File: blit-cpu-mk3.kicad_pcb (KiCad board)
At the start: 4 copper layers, 100 x 80 mm, 169 parts, among them J1 SYS, J11 nML out, J12 nVP out, J13 phi1/abort, J14 nSO in, J16 SYS AUX, J31 HDMI_C_1.3, J32 sound, J33 soundraw, J41 μSD, J44 i2c, J51 rpi_gpio, J52 Conn_02x20_Odd_Even, J54 Conn_02x08_Odd_Even, J56 BOOT, J57 rpi power, J81 JTAG, J82 Jumper, J91 AUX/SYS PWR, J92 AUX PWR, SW611 user0, SW612 user1, SW81 nConfig, U11 74LVC4245A, U12 74LVC4245A, U13 74LVC4245A, U14 74LVC4245A, U21 sst39x040, U22 generic_2048x8_TSOP_II_44, U23 generic_2048x8_TSOP_II_44, U24 generic_2048x8_TSOP_II_44, U25 generic_2048x8_TSOP_II_44, U31 tpd12s016, U42 24AA64-I_OT, U43 rtc_mc_rv_8263_c7, U51 74LVC4245A, U52 74LVC4245A, U53 74CB3T16211, U54 74CB3T16211, U55 74CB3T16211, U8 10M16DCF256I7G_mk3pinstest, U91 stm795, U92 TPS3808, U93 LM1117-1.2, U94 LM1117-2.5, U95 LM1117-3.3, X96 SIT1602BC-23-25N-48.000000

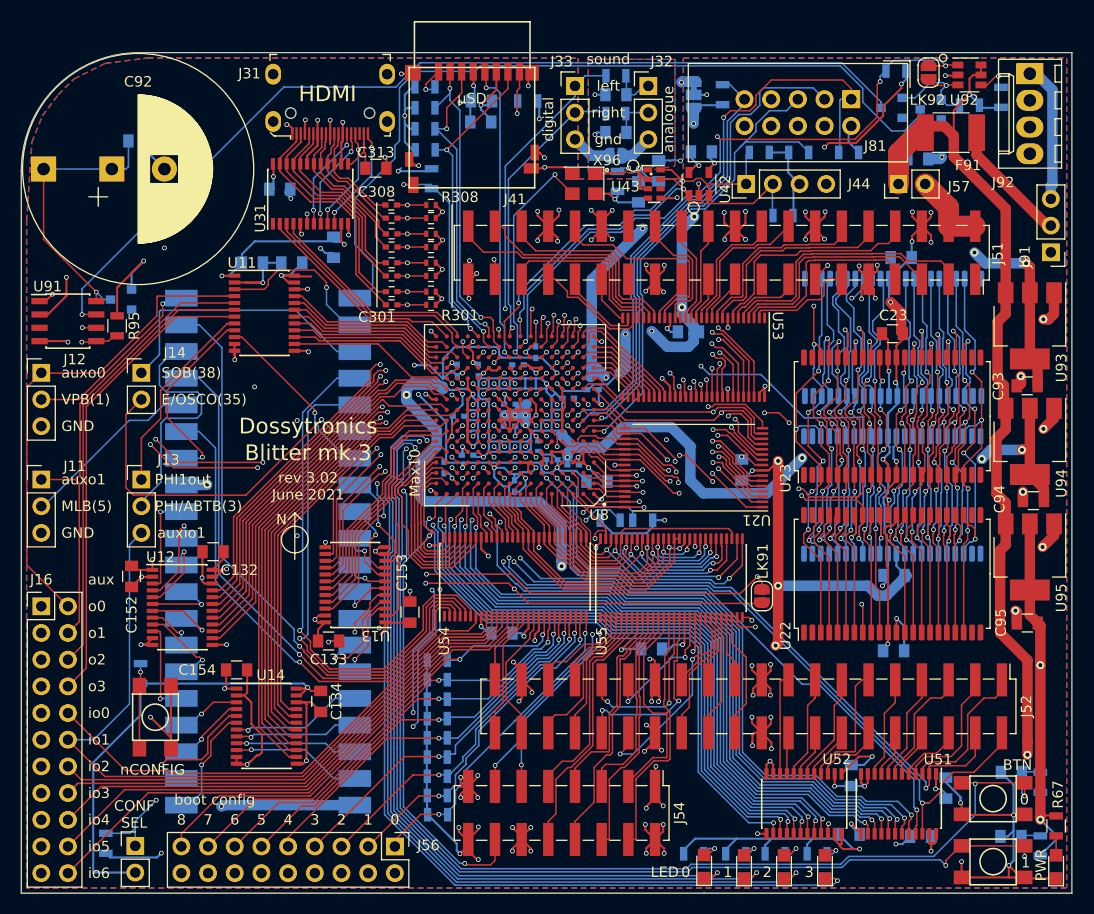
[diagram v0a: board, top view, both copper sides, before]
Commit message: Mk.3 fixes and new 68000 expansion board
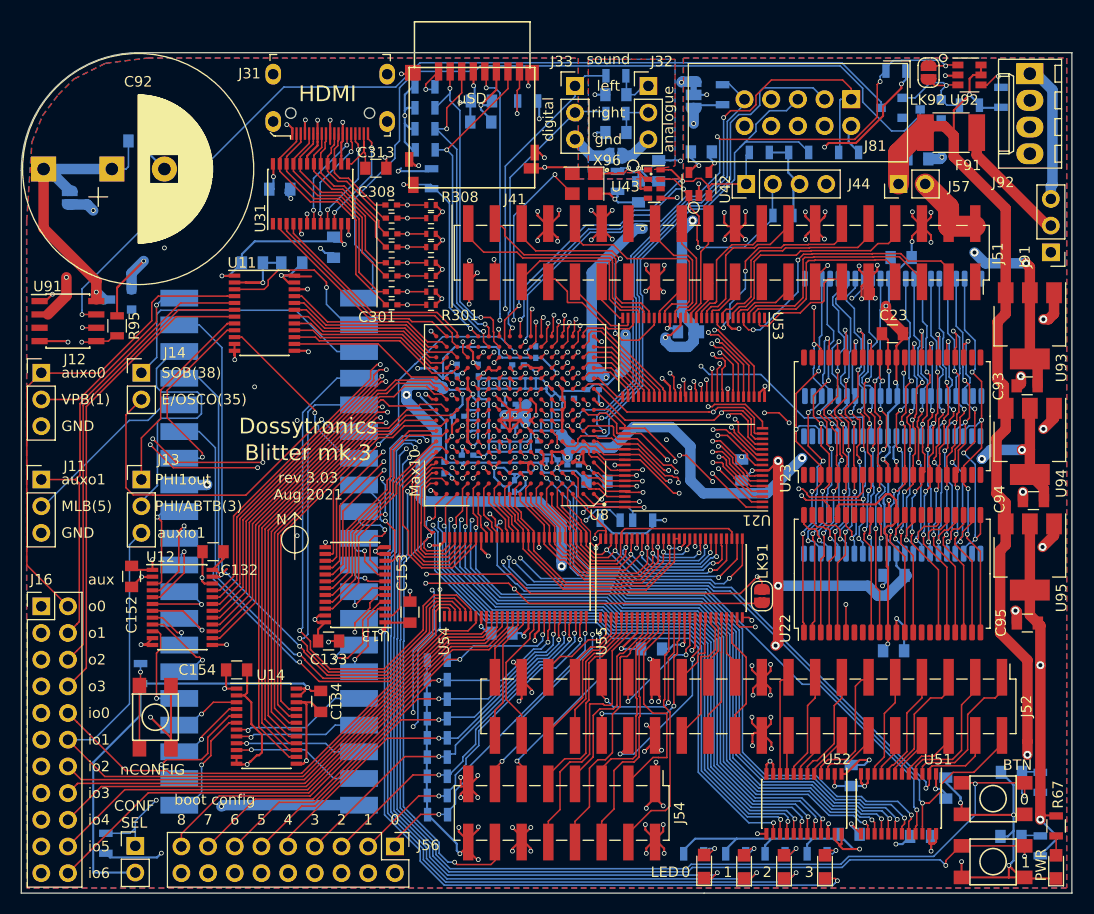
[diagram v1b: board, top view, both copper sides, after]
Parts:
- added LK90: NF, mk3blit:SolderJumper-2_P1.3mm_Open_RoundedPad1.0x1.5mm-domsmallctyd, B.Cu at (26.6, 35.8)
- R63, R64, R65, R66, R67: value 4k7 -> 2k2
- U22: value generic_2048x8_TSOP_II_44 -> generic_2048x8_TSOP_II_44_BB
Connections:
- U22 pad 1: Net-(U22-Pad1) -> /memory/MEM_A14
- U22 pad 15: /MEM_nWE -> Net-(U22-Pad15)
- U22 pad 16: /memory/MEM_A3 -> Net-(U22-Pad16)
- U22 pad 17: /memory/MEM_A2 -> /MEM_nWE
- U22 pad 18: /memory/MEM_A1 -> /memory/MEM_A3
- U22 pad 19: /memory/MEM_A0 -> /memory/MEM_A2
- U22 pad 2: Net-(U22-Pad2) -> /memory/MEM_A13
- U22 pad 20: /memory/MEM_A10 -> /memory/MEM_A1
- U22 pad 21: Net-(U22-Pad21) -> /memory/MEM_A0
- U22 pad 22: Net-(U22-Pad22) -> /memory/MEM_A10
- U22 pad 23: Net-(U22-Pad23) -> /memory/MEM_A19
- U22 pad 24: Net-(U22-Pad24) -> /memory/MEM_A4
- U22 pad 25: /memory/MEM_A19 -> /memory/MEM_A5
- U22 pad 26: /memory/MEM_A4 -> /memory/MEM_A6
- U22 pad 27: /memory/MEM_A5 -> /memory/MEM_A7
- U22 pad 28: /memory/MEM_A6 -> /memory/MEM_A12
- U22 pad 29: /memory/MEM_A7 -> Net-(U22-Pad29)
- U22 pad 3: /memory/MEM_A14 -> /memory/MEM_A8
- U22 pad 30: /memory/MEM_A12 -> Net-(U22-Pad30)
- U22 pad 37: /MEM_nOE -> Net-(U22-Pad37)
- U22 pad 38: /memory/MEM_A17 -> Net-(U22-Pad38)
- U22 pad 39: /memory/MEM_A15 -> /memory/MEM_A17
- U22 pad 4: /memory/MEM_A13 -> /memory/MEM_A9
- U22 pad 40: /memory/MEM_A16 -> /memory/RAM0PWR
- U22 pad 41: /memory/MEM_A18 -> /MEM_nOE
- U22 pad 42: /memory/MEM_A20 -> /memory/MEM_A15
- U22 pad 43: Net-(U22-Pad43) -> /memory/MEM_A16
- U22 pad 44: Net-(U22-Pad44) -> /memory/MEM_A18
- U22 pad 5: /memory/MEM_A8 -> /memory/MEM_A11
- U22 pad 6: /memory/MEM_A9 -> /MEM_BB_nCE_BB
- U22 pad 7: /memory/MEM_A11 -> Net-(U22-Pad7)
- U22 pad 8: /MEM_BB_nCE_BB -> Net-(U22-Pad8)
- U8 pad G1: /fpga_power/~ALTERA_TMS~ -> /fpga_power/~ALTERA_TDI~
- U8 pad H2: /fpga_power/~ALTERA_TDI~ -> /fpga_power/~ALTERA_TMS~
- U8 pad J11: /sys_plug_and_buffers/SYS_D0 -> /CLK_48M
- U8 pad P8: /CLK_48M -> /sys_plug_and_buffers/SYS_D0
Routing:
- net /CLK_48M: track 22.0 -> 31.0 mm, vias 2 -> 3
- net /memory/RAM0PWR: track 99.9 -> 108.8 mm
- net /sys_plug_and_buffers/SYS_D0: track 25.1 -> 33.9 mm
- net /expansion_headers/5_exp_PORTD9: track 19.3 -> 23.8 mm, vias 0 -> 2
- net /I2C_SCL: track 39.5 -> 44.0 mm, vias 2 -> 3
- net /power/VBAT: track 26.8 -> 30.1 mm
- net /fpga_power/~ALTERA_TMS~: track 49.3 -> 52.5 mm
- net /memory/MEM_A20: track 62.7 -> 59.9 mm
- net +3V3BB: track 97.9 -> 100.4 mm, vias 4 -> 5
- net /memory/MEM_A4: track 79.9 -> 77.6 mm
- net GND: track 1473.9 -> 1471.8 mm
- net /sys_plug_and_buffers/5C_SYS_D1: track 7.48 -> 9.51 mm
- net /memory/MEM_A12: track 77.4 -> 79.1 mm
- net /memory/MEM_A15: track 72.2 -> 73.8 mm
- net /memory/MEM_A1: track 76.5 -> 78.0 mm
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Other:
- board text added: "rev 3.03 Aug 2021"
- board text removed: "rev 3.02 June 2021"
